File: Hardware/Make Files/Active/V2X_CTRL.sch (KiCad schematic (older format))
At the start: 38 parts, among them CON1 AVR-PDI-6, IC1 ATXMEGA16A4U-A, P20 Jumper 1, P21 Jumper 2, P22 CONN_02X04, P23 Jumper 3, P24 Jumper 4, Q16 2N7000, Q17 2N7000, Q18 2N7000, Q19 2N7000, U21 74LS126, U22 74HC595, U23 74HC595

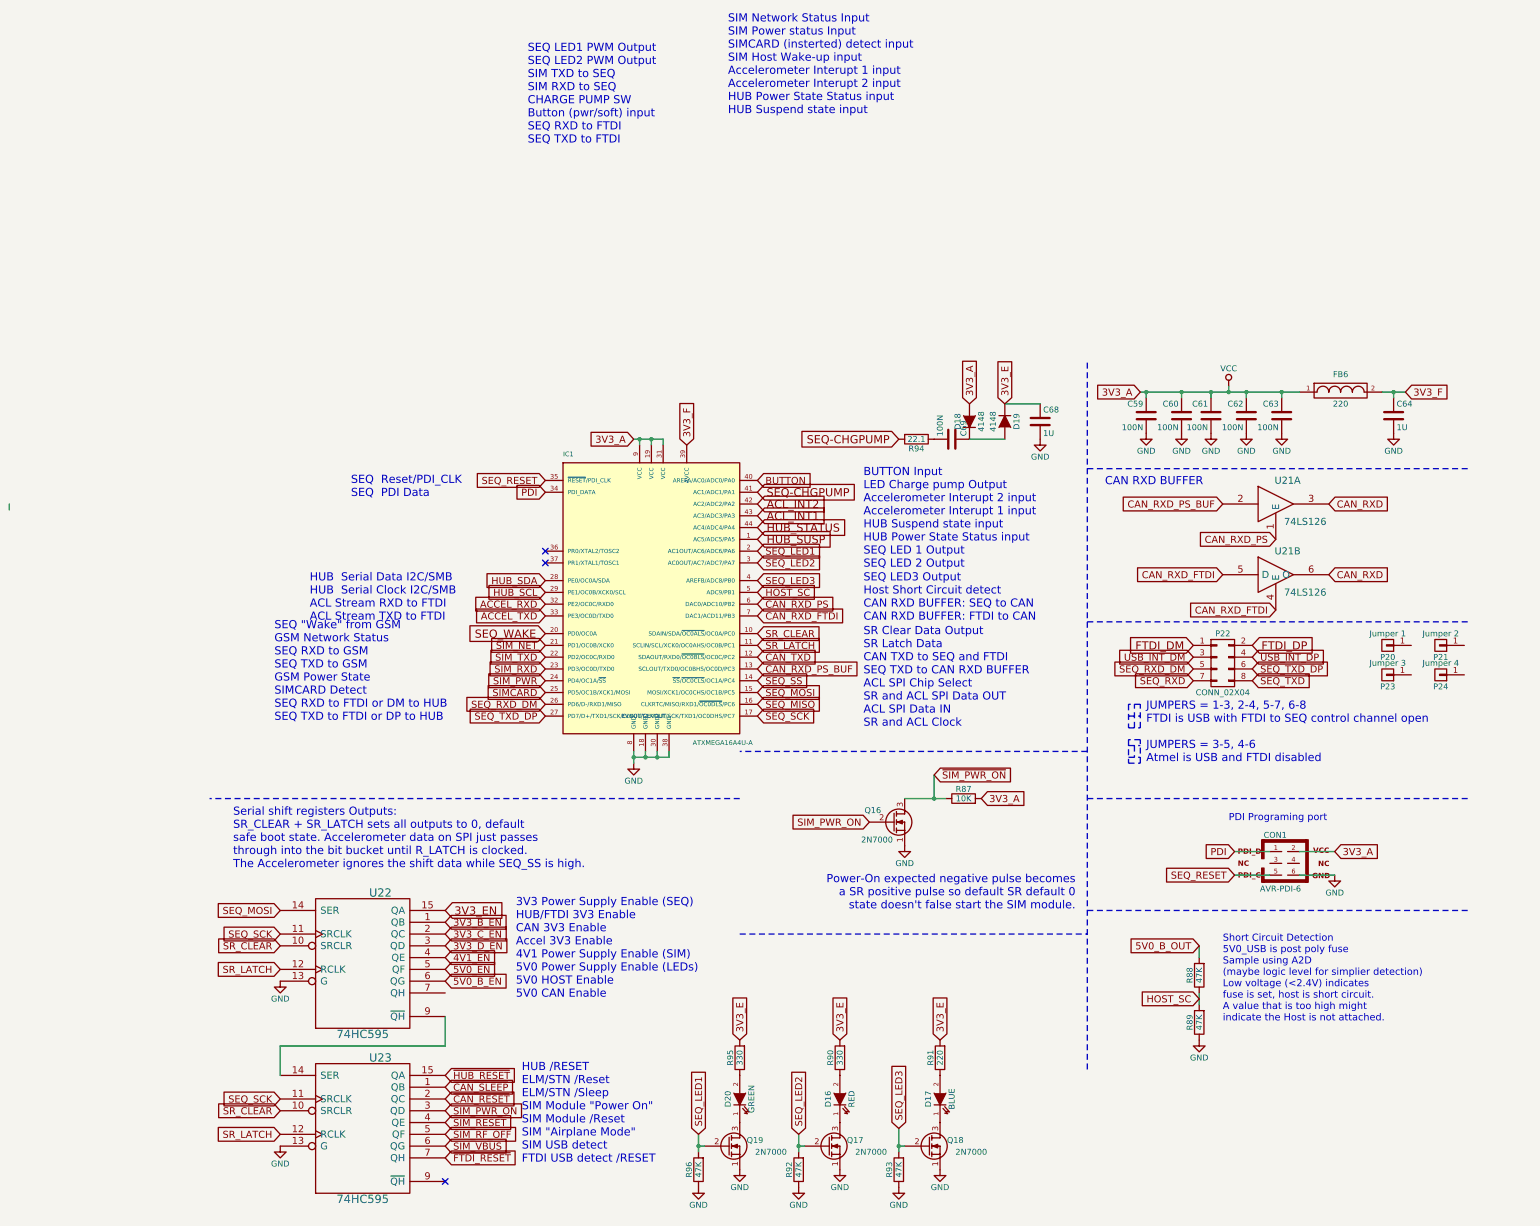
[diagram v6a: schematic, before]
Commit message: Added USB-A to design
discovered the Rpi cannot be back fed over USB, had to add a power Port
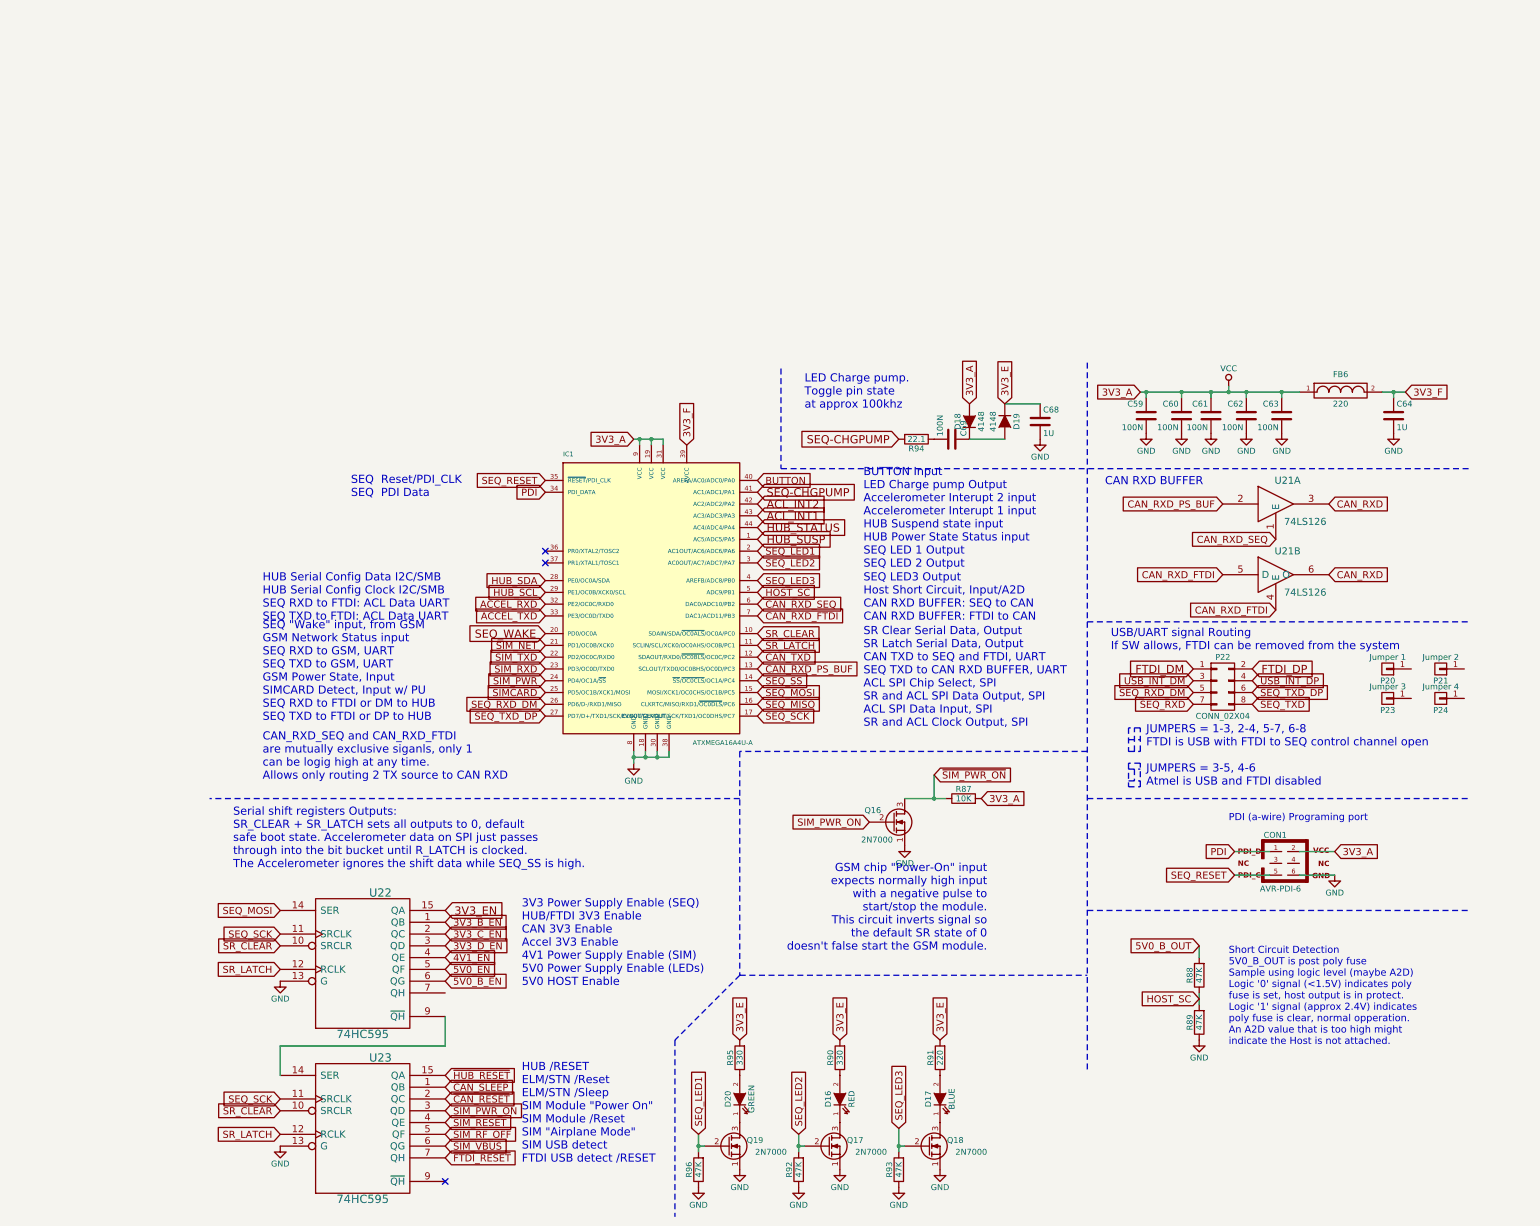
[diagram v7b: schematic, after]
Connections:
- net labels added: CAN_RXD_SEQ
- net labels removed: CAN_RXD_PS
- wire segments 38 -> 37
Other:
- note added: "3V3 Power Supply Enable (SEQ)\nHUB/FTDI 3V3 Enable\nCAN 3V3 Enable\nAccel 3V3 Enable\n4V1 Power Supply Enable (SIM)\n5V0 Power Supply Enable (LEDs)\n5V0 HOST Enable \n"
- note added: "CAN_RXD_SEQ and CAN_RXD_FTDI\nare mutually exclusive siganls, only 1\ncan be logig high at any time.\nAllows only routing 2 TX source to CAN RXD"
- note added: "GSM chip "Power-On" input\nexpects normally high input\nwith a negative pulse to \nstart/stop the module.\nThis circuit inverts signal so \nthe default SR state of 0 \ndoesn't false start the GSM module."
- note added: "HUB Serial Config Data I2C/SMB\nHUB Serial Config Clock I2C/SMB\nSEQ RXD to FTDI: ACL Data UART\nSEQ TXD to FTDI: ACL Data UART"
- note added: "LED Charge pump. \nToggle pin state \nat approx 100khz"
- note added: "PDI (a-wire) Programing port"
- note added: "SEQ "Wake" input, from GSM\nGSM Network Status input\nSEQ RXD to GSM, UART \nSEQ TXD to GSM, UART\nGSM Power State, Input\nSIMCARD Detect, Input w/ PU\nSEQ RXD to FTDI or DM to HUB\nSEQ TXD to FTDI or DP to HUB"
- note added: "SEQ LED3 Output\nHost Short Circuit, Input/A2D\nCAN RXD BUFFER: SEQ to CAN \nCAN RXD BUFFER: FTDI to CAN"
- note added: "SR Clear Serial Data, Output\nSR Latch Serial Data, Output\nCAN TXD to SEQ and FTDI, UART\nSEQ TXD to CAN RXD BUFFER, UART\nACL SPI Chip Select, SPI\nSR and ACL SPI Data Output, SPI\nACL SPI Data Input, SPI\nSR and ACL Clock Output, SPI"
- note added: "Short Circuit Detection\n5V0_B_OUT is post poly fuse\nSample using logic level (maybe A2D)\nLogic '0' signal (<1.5V) indicates poly\nfuse is set, host output is in protect.\nLogic '1' signal (approx 2.4V) indicates\npoly fuse is clear, normal opperation.\nAn A2D value that is too high might \nindicate the Host is not attached."
- note added: "USB/UART signal Routing\nIf SW allows, FTDI can be removed from the system"
- note removed: "3V3 Power Supply Enable (SEQ)\nHUB/FTDI 3V3 Enable\nCAN 3V3 Enable\nAccel 3V3 Enable\n4V1 Power Supply Enable (SIM)\n5V0 Power Supply Enable (LEDs)\n5V0 HOST Enable \n5V0 CAN Enable"
- note removed: "HUB Serial Data I2C/SMB\nHUB Serial Clock I2C/SMB\nACL Stream RXD to FTDI\nACL Stream TXD to FTDI"
- note removed: "PDI Programing port"
- note removed: "Power-On expected negative pulse becomes \na SR positive pulse so default SR default 0 \nstate doesn't false start the SIM module."
- note removed: "SEQ "Wake" from GSM\nGSM Network Status\nSEQ RXD to GSM\nSEQ TXD to GSM\nGSM Power State\nSIMCARD Detect\nSEQ RXD to FTDI or DM to HUB\nSEQ TXD to FTDI or DP to HUB"
- note removed: "SEQ LED1 PWM Output\nSEQ LED2 PWM Output\nSIM TXD to SEQ\nSIM RXD to SEQ\nCHARGE PUMP SW\nButton (pwr/soft) input\nSEQ RXD to FTDI\nSEQ TXD to FTDI"
- note removed: "SEQ LED3 Output\nHost Short Circuit detect\nCAN RXD BUFFER: SEQ to CAN \nCAN RXD BUFFER: FTDI to CAN"
- note removed: "SIM Network Status Input\nSIM Power status Input\nSIMCARD (insterted) detect input\nSIM Host Wake-up input\nAccelerometer Interupt 1 input\nAccelerometer Interupt 2 input\nHUB Power State Status input\nHUB Suspend state input"
- note removed: "SR Clear Data Output\nSR Latch Data \nCAN TXD to SEQ and FTDI\nSEQ TXD to CAN RXD BUFFER\nACL SPI Chip Select\nSR and ACL SPI Data OUT\nACL SPI Data IN\nSR and ACL Clock"
- note removed: "Short Circuit Detection\n5V0_USB is post poly fuse\nSample using A2D \n(maybe logic level for simplier detection)\nLow voltage (<2.4V) indicates\nfuse is set, host is short circuit.\nA value that is too high might \nindicate the Host is not attached."
- moved on the sheet: P20, P21, P22, P23, P24

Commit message: No Rpi Backpower fix
added a USB-A to the board to power the HOST. fixed LED labeling.
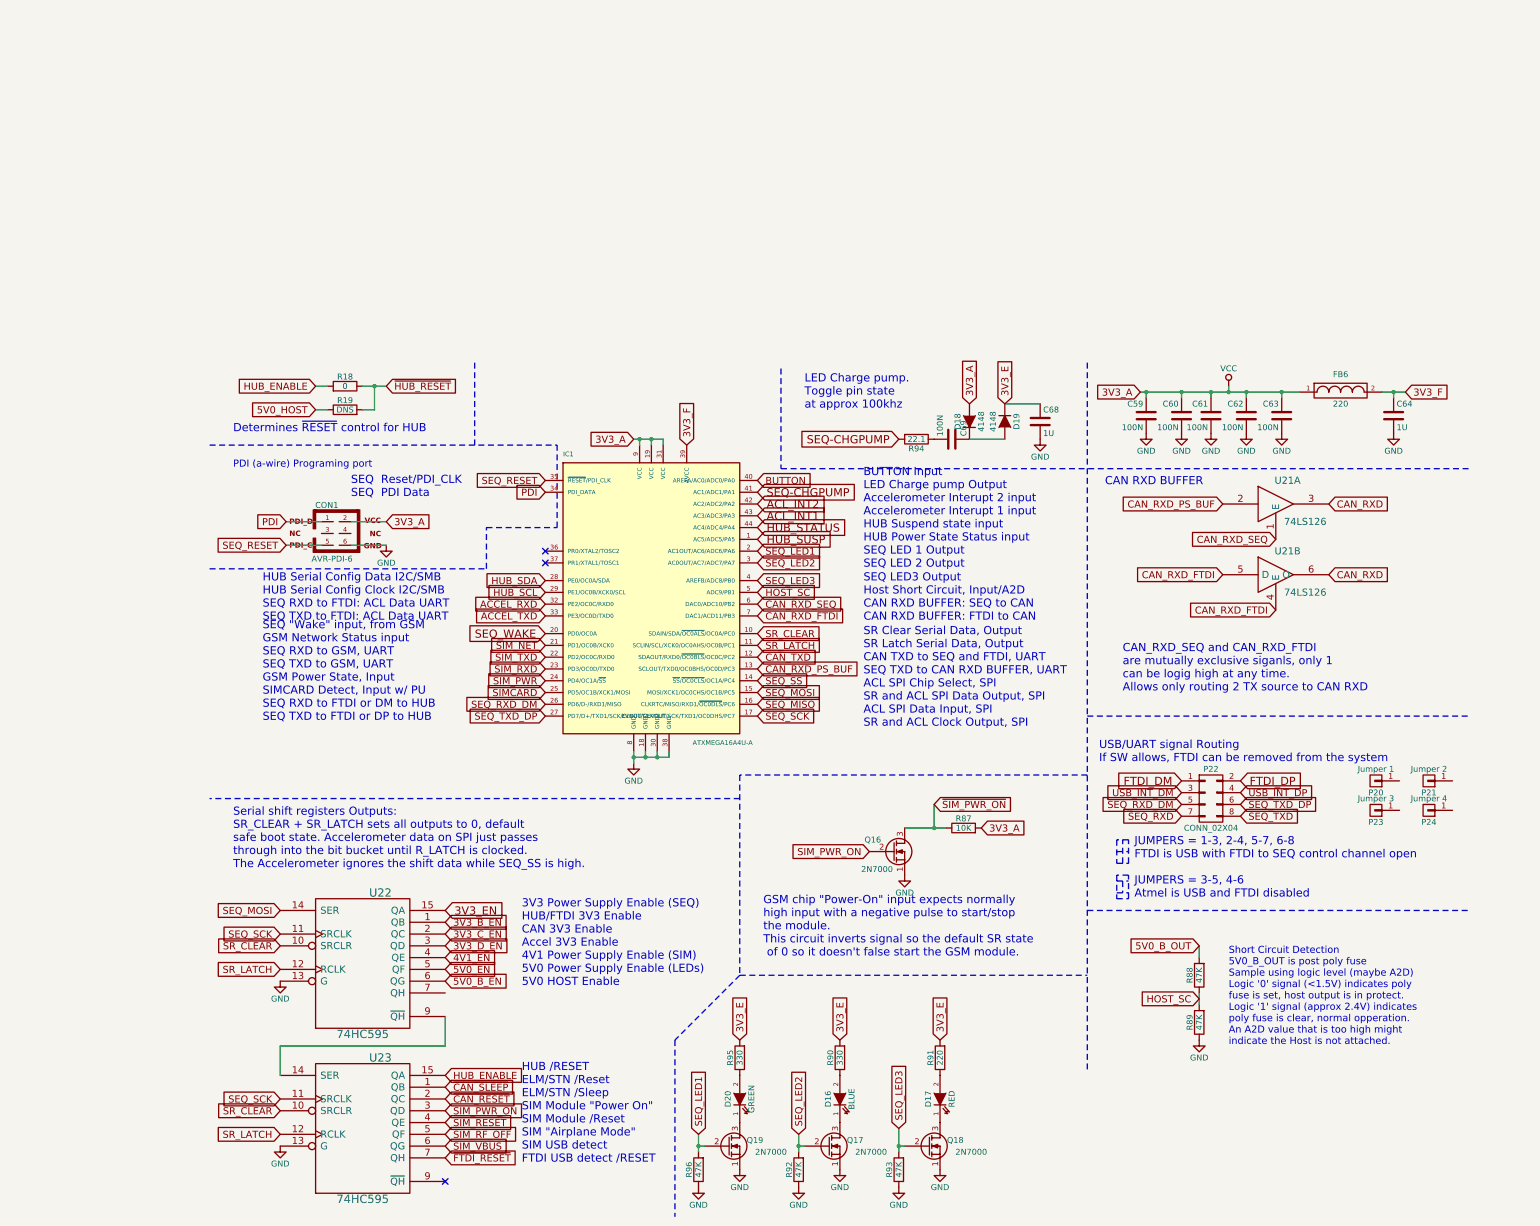
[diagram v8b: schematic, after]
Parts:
- added R18: 0, Custom Parts:R_0603_sm, symbol R
- added R19: DNS, Custom Parts:R_0603_sm, symbol R
- D16: value RED -> BLUE
- D17: value BLUE -> RED
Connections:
- net ~HUB_RESET: now also R18.1, R19.2; no longer U23.15 (QA)
- new net 5V0_HOST: R19.1
- new net HUB_ENABLE: R18.2, U23.15 (QA)
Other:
- note added: "Determines ~RESET~ control for HUB"
- note added: "GSM chip "Power-On" input expects normally \nhigh input with a negative pulse to start/stop \nthe module.\nThis circuit inverts signal so the default SR state\n of 0 so it doesn't false start the GSM module."
- note removed: "GSM chip "Power-On" input\nexpects normally high input\nwith a negative pulse to \nstart/stop the module.\nThis circuit inverts signal so \nthe default SR state of 0 \ndoesn't false start the GSM module."
- moved on the sheet: CON1, P20, P21, P22, P23, P24, Q16, R87
